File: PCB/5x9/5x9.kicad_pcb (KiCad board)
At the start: 2 copper layers, 10 x 22 mm, 57 parts, among them J1 Conn_01x03, J2 Conn_01x03

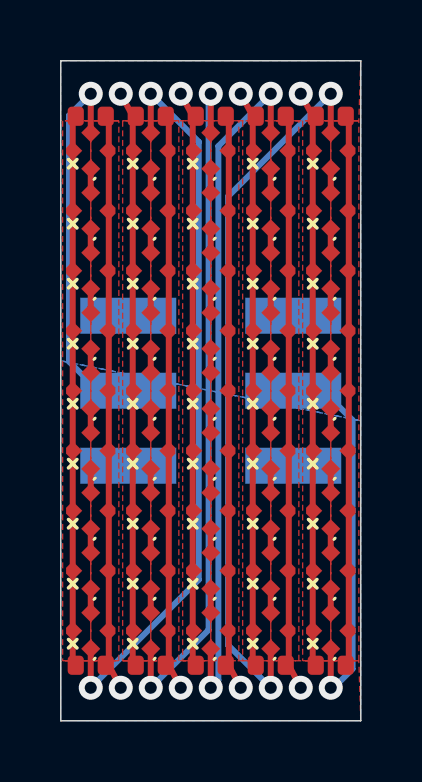
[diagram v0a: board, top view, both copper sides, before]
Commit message: Change pads
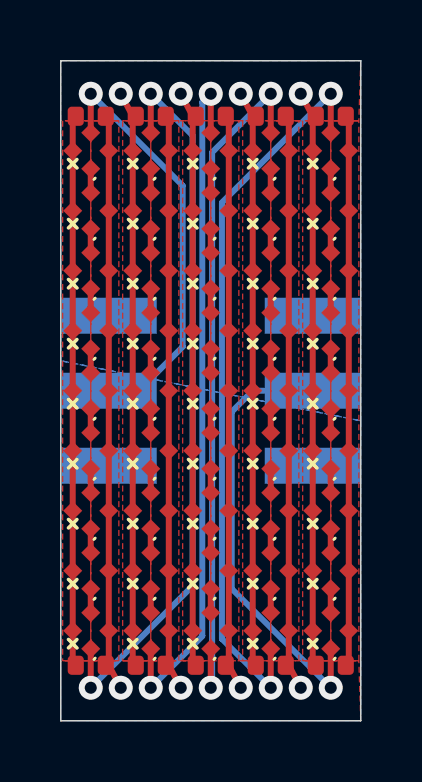
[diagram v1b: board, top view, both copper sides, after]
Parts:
- moved J1 0.65 mm to (101.6, 89.0)
- moved J2 0.65 mm to (108.4, 89.0)
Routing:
- net Net-(D45-O): track 13.0 -> 14.9 mm
- net Net-(D1-I): track 12.9 -> 14.1 mm

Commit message: New footprint on LEDs
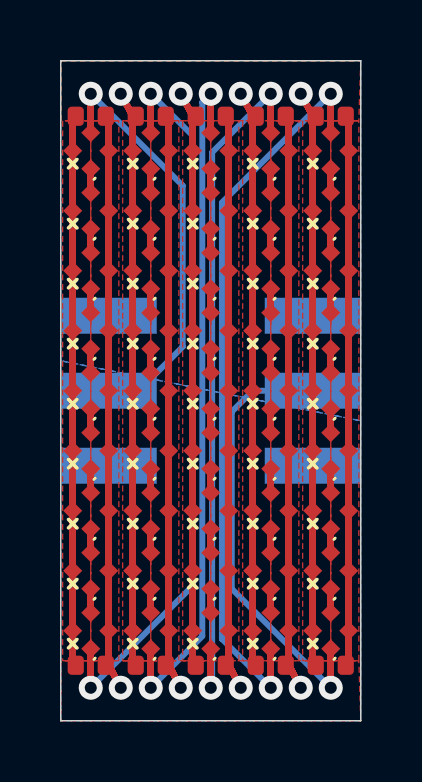
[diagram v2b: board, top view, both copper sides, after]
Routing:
- net (no net): track 0.00 -> 8201.0 mm, vias 0 -> 18
- net VCC: vias 4 -> 0
- net Net-(D45-O): vias 1 -> 0
- net Net-(D36-O): vias 2 -> 0
- net Net-(D27-O): vias 2 -> 0
- net Net-(D18-O): vias 2 -> 0
- net Net-(D10-I): vias 2 -> 0
- net Net-(D1-I): vias 1 -> 0
- net GND: vias 4 -> 0
